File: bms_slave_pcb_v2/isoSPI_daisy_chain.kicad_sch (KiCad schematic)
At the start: 10 parts

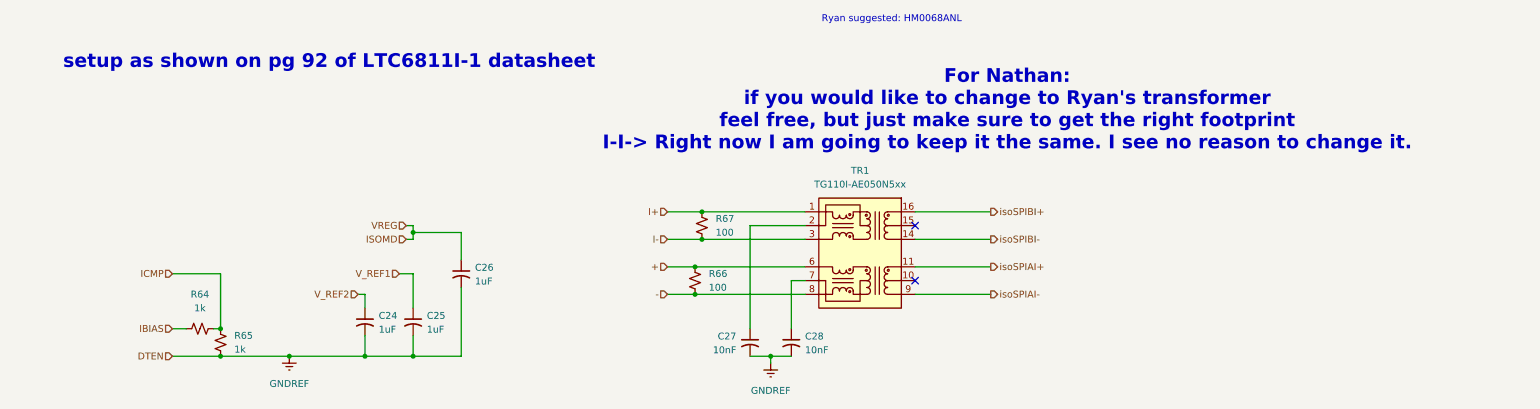
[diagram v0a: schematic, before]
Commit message: Fixed filenames in BMS Slave PCB V2.01, added equipment wishlist
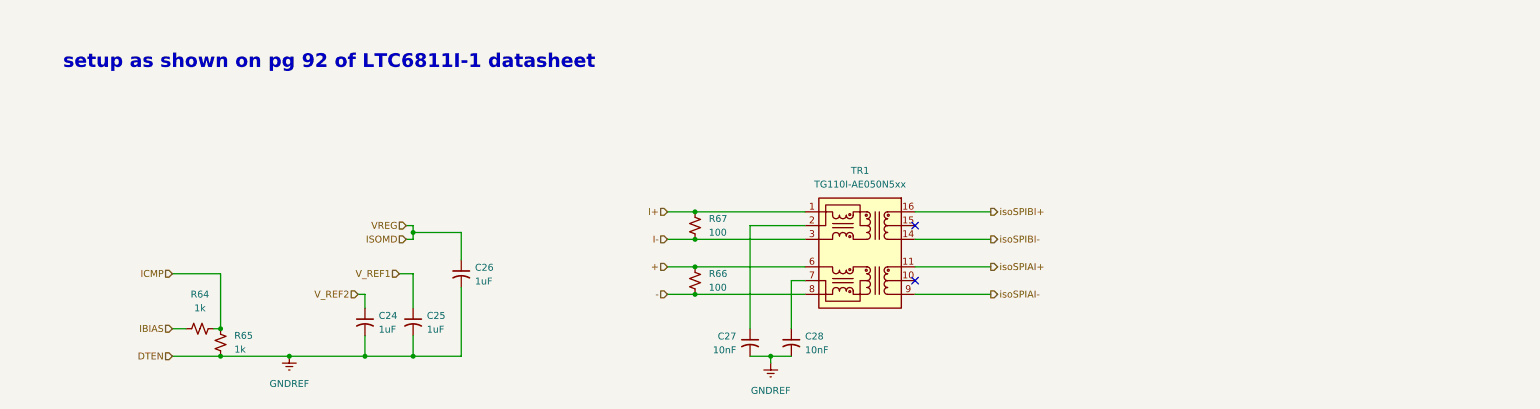
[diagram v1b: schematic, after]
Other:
- note removed: "For Nathan: if you would like to change to Ryan's transformer feel free, but just make sure to get the right footprint I-I-> Right now I am going to keep it the same. I see no reason to change it."
- note removed: "Ryan suggested: HM0068ANL"
- moved on the sheet: R67
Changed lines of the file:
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@@
 		(comment 1 "Designed by: Rugby Taylor, Carson Coleman, Nathan Christiansen")
-	)
-	(text "For Nathan:\nif you would like to change to Ryan's transformer\nfeel free, but just make sure to get the right footprint\nI-I-> Right now I am going to keep it the same. I see no reason to change it."
-		(exclude_from_sim no)
-		(at 198.628 33.274 0)
-		(effects
-			(font
-				(size 2.54 2.54)
-				(thickness 0.508)
-				(bold yes)
-			)
-		)
 	)
 	(text "setup as shown on pg 92 of LTC6811I-1 datasheet"
@@
 		)
 	)
-	(text "Ryan suggested: HM0068ANL"
-		(exclude_from_sim no)
-		(at 177.292 16.51 0)
-		(effects
-			(font
-				(size 1.27 1.27)
-			)
-		)
-	)
 	(junction
 		(at 140.97 67.31)
@@
 	)
 	(junction
+		(at 140.97 52.07)
+		(diameter 0)
+		(color 0 0 0 0)
+	)
+	(junction
 		(at 140.97 62.23)
 		(diameter 0)
@@
 	)
 	(junction
-		(at 142.24 52.07)
+		(at 140.97 57.15)
 		(diameter 0)
 		(color 0 0 0 0)
@@
 	)
 	(junction
-		(at 142.24 57.15)
-		(diameter 0)
-		(color 0 0 0 0)
-	)
-	(junction
 		(at 154.94 78.74)
 		(diameter 0)
@@
 	(wire
 		(pts
-			(xy 135.89 57.15) (xy 142.24 57.15)
+			(xy 135.89 57.15) (xy 140.97 57.15)
 		)
 		(stroke
@@
 	(wire
 		(pts
+			(xy 140.97 52.07) (xy 161.29 52.07)
+		)
+		(stroke
+			(width 0)
+			(type default)
+		)
+	)
+	(wire
+		(pts
 			(xy 80.01 67.31) (xy 80.01 69.85)
 		)
@@
 	(wire
 		(pts
-			(xy 142.24 52.07) (xy 161.29 52.07)
-		)
-		(stroke
-			(width 0)
-			(type default)
-		)
-	)
-	(wire
-		(pts
 			(xy 158.75 64.77) (xy 161.29 64.77)
 		)
@@
 	(wire
 		(pts
-			(xy 142.24 57.15) (xy 161.29 57.15)
-		)
-		(stroke
-			(width 0)
-			(type default)
-		)
-	)
-	(wire
-		(pts
 			(xy 154.94 78.74) (xy 154.94 80.01)
 		)
@@
 	(wire
 		(pts
-			(xy 135.89 52.07) (xy 142.24 52.07)
+			(xy 135.89 52.07) (xy 140.97 52.07)
 		)
 		(stroke
@@
 		(pts
 			(xy 53.34 78.74) (xy 66.04 78.74)
+		)
+		(stroke
+			(width 0)
+			(type default)
+		)
+	)
+	(wire
+		(pts
+			(xy 140.97 57.15) (xy 161.29 57.15)
 		)
 		(stroke
@@
 		)
 		(instances
-			(project "bms_slave_pcb"
+			(project "bms_slave_pcb_V2.01"
 				(path "/41ccf350-ee7b-4386-b0cf-c25b52556b27/33276a2f-22a9-4a64-97a7-172a4edf84ea"
 					(reference "C24")
@@
 		)
 		(instances
-			(project "bms_slave_pcb"
+			(project "bms_slave_pcb_V2.01"
 				(path "/41ccf350-ee7b-4386-b0cf-c25b52556b27/33276a2f-22a9-4a64-97a7-172a4edf84ea"
 					(reference "TR1")
@@
 		)
 		(instances
-			(project "bms_slave_pcb"
+			(project "bms_slave_pcb_V2.01"
 				(path "/41ccf350-ee7b-4386-b0cf-c25b52556b27/33276a2f-22a9-4a64-97a7-172a4edf84ea"
 					(reference "R64")
@@
 		)
 		(instances
-			(project "bms_slave_pcb"
+			(project "bms_slave_pcb_V2.01"
 				(path "/41ccf350-ee7b-4386-b0cf-c25b52556b27/33276a2f-22a9-4a64-97a7-172a4edf84ea"
 					(reference "C28")
@@
 	(symbol
 		(lib_id "Device:R_Small_US")
-		(at 142.24 54.61 180)
+		(at 140.97 54.61 180)
 		(unit 1)
 		(body_style 1)
@@
 		(fields_autoplaced yes)
 		(property "Reference" "R67"
-			(at 144.78 53.3399 0)
+			(at 143.51 53.3399 0)
 			(show_name no)
 			(do_not_autoplace no)
@@
 		)
 		(property "Value" "100"
-			(at 144.78 55.8799 0)
+			(at 143.51 55.8799 0)
 			(show_name no)
 			(do_not_autoplace no)
@@
 		)
 		(property "Footprint" "Resistor_SMD:R_0805_2012Metric_Pad1.20x1.40mm_HandSolder"
-			(at 142.24 54.61 0)
+			(at 140.97 54.61 0)
 			(hide yes)
 			(show_name no)
@@
 		)
 		(property "Datasheet" ""
-			(at 142.24 54.61 0)
+			(at 140.97 54.61 0)
 			(hide yes)
 			(show_name no)
@@
 		)
 		(property "Description" "Resistor, small US symbol"
-			(at 142.24 54.61 0)
+			(at 140.97 54.61 0)
 			(hide yes)
 			(show_name no)
@@
 		)
 		(instances
-			(project "bms_slave_pcb"
+			(project "bms_slave_pcb_V2.01"
 				(path "/41ccf350-ee7b-4386-b0cf-c25b52556b27/33276a2f-22a9-4a64-97a7-172a4edf84ea"
 					(reference "R67")
@@
 		)
 		(instances
-			(project "bms_slave_pcb"
+			(project "bms_slave_pcb_V2.01"
 				(path "/41ccf350-ee7b-4386-b0cf-c25b52556b27/33276a2f-22a9-4a64-97a7-172a4edf84ea"
 					(reference "R66")
@@
 		)
 		(instances
-			(project "bms_slave_pcb"
+			(project "bms_slave_pcb_V2.01"
 				(path "/41ccf350-ee7b-4386-b0cf-c25b52556b27/33276a2f-22a9-4a64-97a7-172a4edf84ea"
 					(reference "C27")
@@
 		)
 		(instances
-			(project "bms_slave_pcb"
+			(project "bms_slave_pcb_V2.01"
 				(path "/41ccf350-ee7b-4386-b0cf-c25b52556b27/33276a2f-22a9-4a64-97a7-172a4edf84ea"
 					(reference "#PWR043")
@@
 		)
 		(instances
-			(project "bms_slave_pcb"
+			(project "bms_slave_pcb_V2.01"
 				(path "/41ccf350-ee7b-4386-b0cf-c25b52556b27/33276a2f-22a9-4a64-97a7-172a4edf84ea"
 					(reference "#PWR042")
@@
 		)
 		(instances
-			(project "bms_slave_pcb"
+			(project "bms_slave_pcb_V2.01"
 				(path "/41ccf350-ee7b-4386-b0cf-c25b52556b27/33276a2f-22a9-4a64-97a7-172a4edf84ea"
 					(reference "C25")
@@
 		)
 		(instances
-			(project "bms_slave_pcb"
+			(project "bms_slave_pcb_V2.01"
 				(path "/41ccf350-ee7b-4386-b0cf-c25b52556b27/33276a2f-22a9-4a64-97a7-172a4edf84ea"
 					(reference "R65")
@@
 		)
 		(instances
-			(project "bms_slave_pcb"
+			(project "bms_slave_pcb_V2.01"
 				(path "/41ccf350-ee7b-4386-b0cf-c25b52556b27/33276a2f-22a9-4a64-97a7-172a4edf84ea"
 					(reference "C26")
